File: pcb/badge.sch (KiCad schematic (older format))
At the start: 17 parts, among them IC101 CH340G, IC102 TP4056, P101 CONN_01X02, P102 USB_OTG, P103 CONN_01X05, x101 xtal_osc

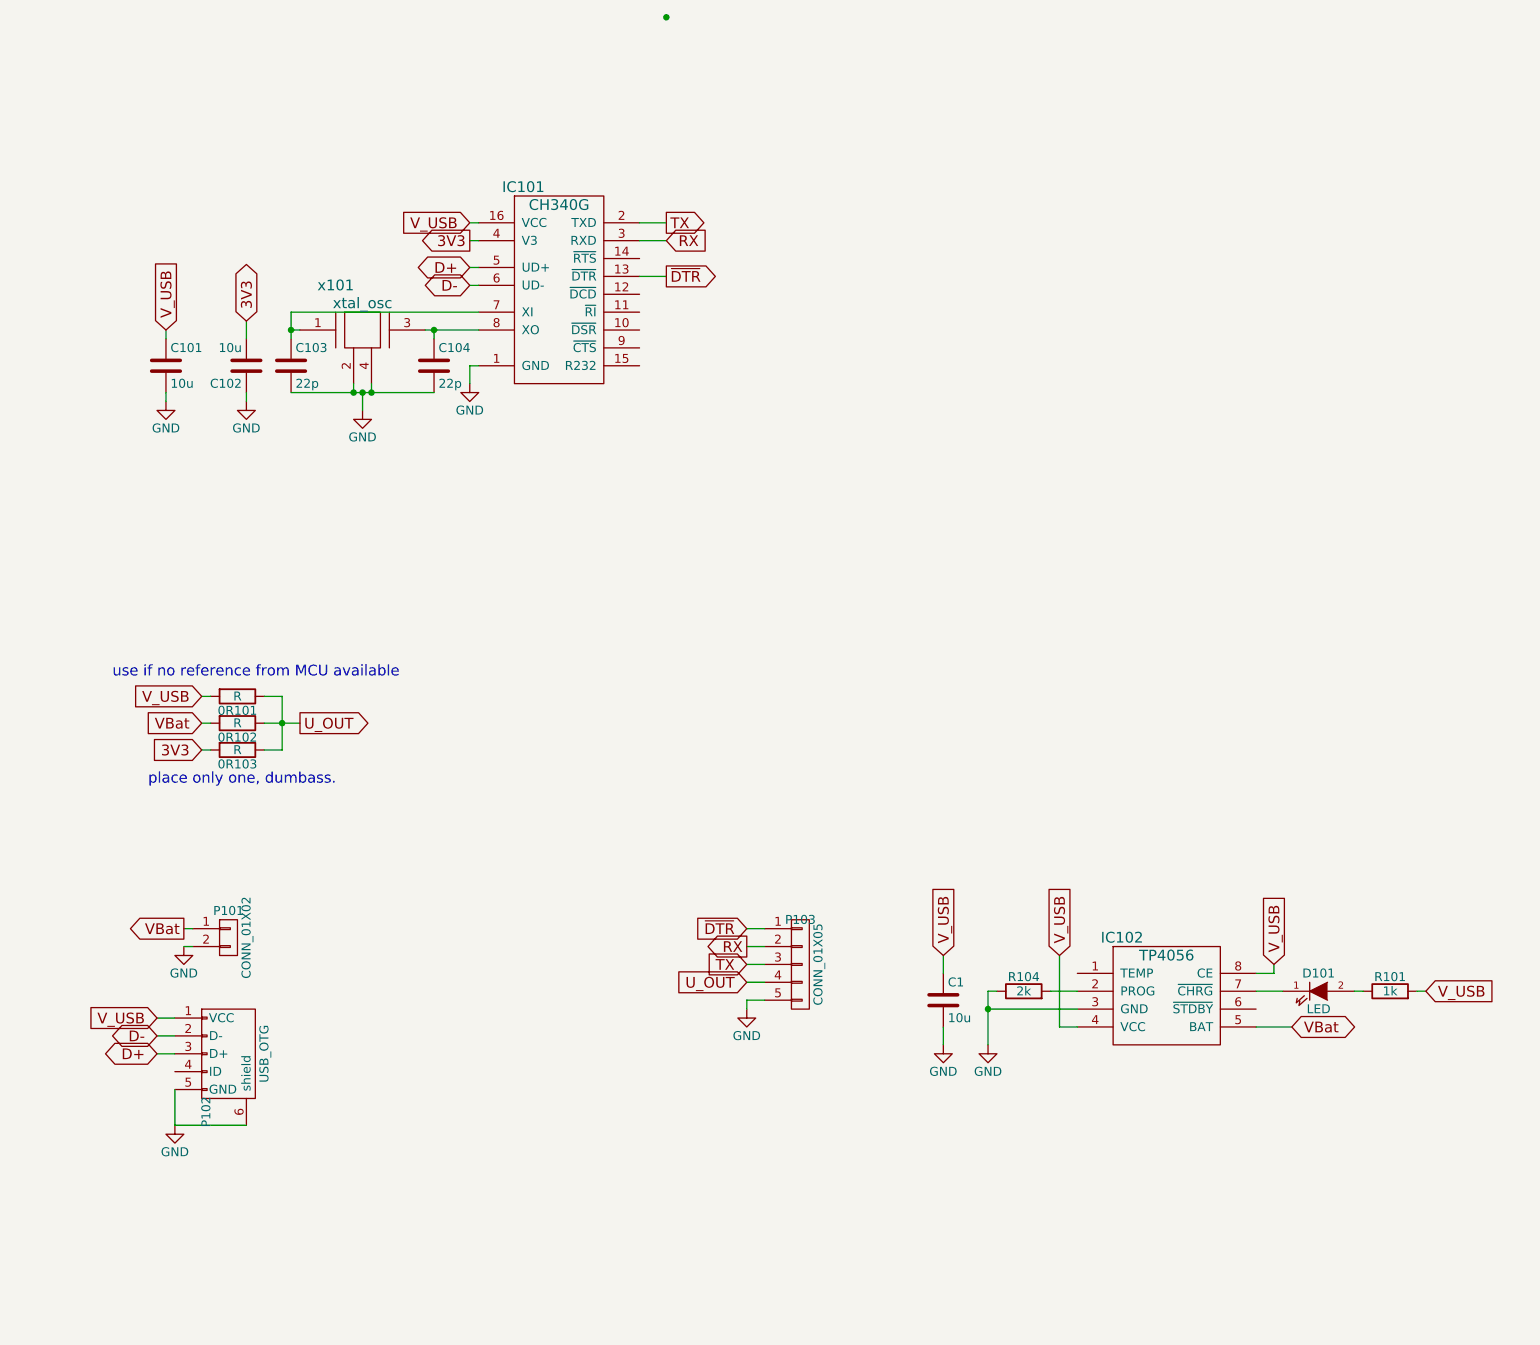
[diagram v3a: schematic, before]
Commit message: updated layout to match schema
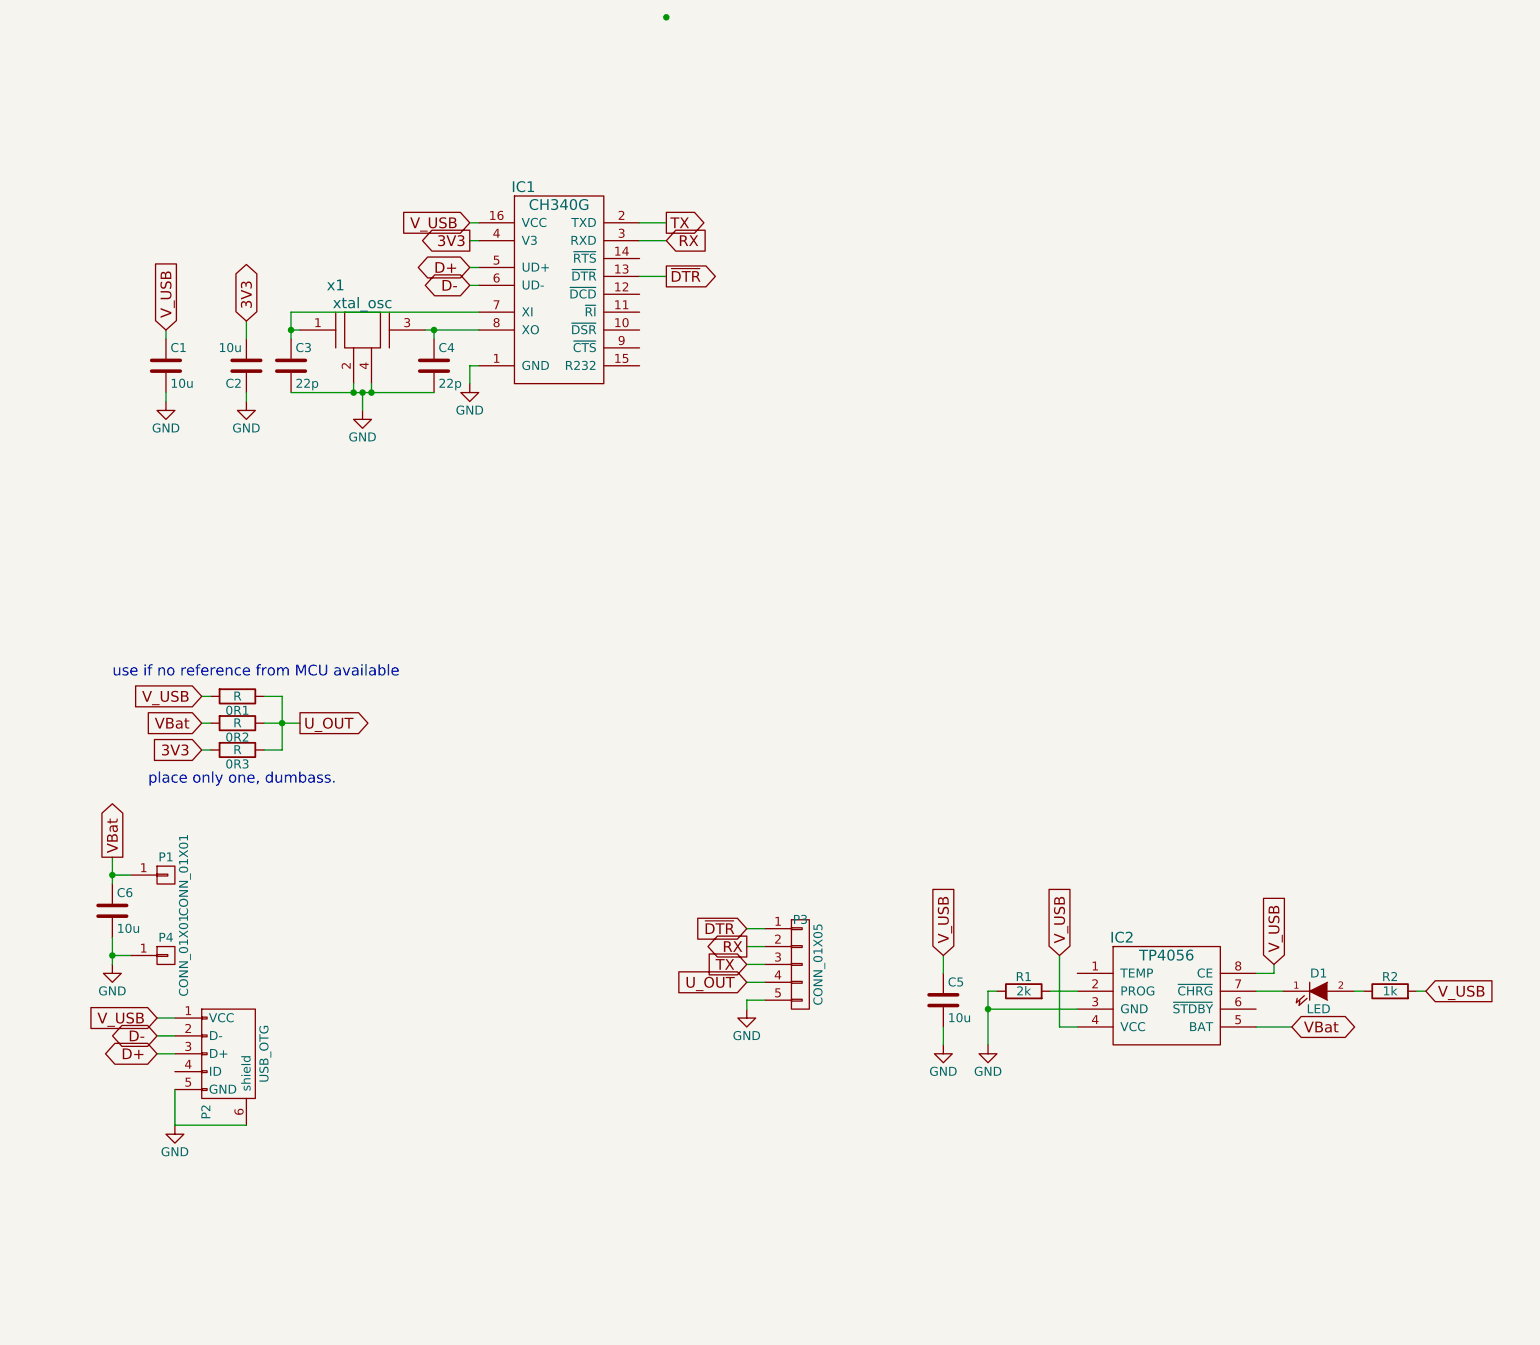
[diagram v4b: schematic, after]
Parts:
- removed P101: CONN_01X02, Pin_Headers:Pin_Header_Straight_1x02, symbol CONN_01X02
- added C6: 10u, netl:SMD_0603, symbol C
- added P1, P4: CONN_01X01, Connect:1pin, symbol CONN_01X01
- renumbered 0R101 to 0R1, 0R102 to 0R2, 0R103 to 0R3, C101 to C1, C102 to C2, C103 to C3, C104 to C4, C1 to C5, D101 to D1, IC101 to IC1, IC102 to IC2, P102 to P2, P103 to P3, R104 to R1, R101 to R2, x101 to x1
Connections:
- net GND: now also C6.2, P4.1 (P1)
- net VBat: now also C6.1, P1.1 (P1)
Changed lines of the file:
@@
 $EndDescr
 $Comp
-L CONN_01X02 P101
-U 1 1 55AEBC12
-P 1700 5450
-F 0 "P101" H 1700 5600 50  0000 C CNN
-F 1 "CONN_01X02" V 1800 5450 50  0000 C CNN
-F 2 "Pin_Headers:Pin_Header_Straight_1x02" H 1700 5450 60  0001 C CNN
-F 3 "" H 1700 5450 60  0000 C CNN
-	1    1700 5450
-	1    0    0    -1
-$EndComp
-Text GLabel 1450 5400 0    60   Output ~ 0
-VBat
-$Comp
-L GND #PWR01
-U 1 1 55AEBCB6
-P 1450 5500
-F 0 "#PWR01" H 1450 5250 50  0001 C CNN
-F 1 "GND" H 1450 5350 50  0000 C CNN
-F 2 "" H 1450 5500 60  0000 C CNN
-F 3 "" H 1450 5500 60  0000 C CNN
-	1    1450 5500
-	1    0    0    -1
-$EndComp
-$Comp
-L USB_OTG P102
+L USB_OTG P2
 U 1 1 55AEBD84
 P 1700 6100
-F 0 "P102" H 2025 5975 50  0000 C CNN
+F 0 "P2" H 2025 5975 50  0000 C CNN
 F 1 "USB_OTG" H 1700 6300 50  0000 C CNN
 F 2 "Connect:USB_Micro-B" V 1650 6000 60  0001 C CNN
@@
 V_USB
 $Comp
-L GND #PWR02
+L GND #PWR01
 U 1 1 55AEBF75
 P 1400 6500
-F 0 "#PWR02" H 1400 6250 50  0001 C CNN
+F 0 "#PWR01" H 1400 6250 50  0001 C CNN
 F 1 "GND" H 1400 6350 50  0000 C CNN
 F 2 "" H 1400 6500 60  0000 C CNN
@@
 D+
 $Comp
-L GND #PWR03
+L GND #PWR02
 U 1 1 579ECB3C
 P 1350 2450
-F 0 "#PWR03" H 1350 2200 50  0001 C CNN
+F 0 "#PWR02" H 1350 2200 50  0001 C CNN
 F 1 "GND" H 1350 2300 50  0000 C CNN
 F 2 "" H 1350 2450 50  0000 C CNN
@@
 $EndComp
 $Comp
-L C C101
+L C C1
 U 1 1 579ECCA5
 P 1350 2250
-F 0 "C101" H 1375 2350 50  0000 L CNN
+F 0 "C1" H 1375 2350 50  0000 L CNN
 F 1 "10u" H 1375 2150 50  0000 L CNN
 F 2 "netl:SMD_0603" H 1388 2100 50  0001 C CNN
@@
 $EndComp
 $Comp
-L CONN_01X05 P103
+L CONN_01X05 P3
 U 1 1 57C2DD7E
 P 4900 5600
-F 0 "P103" H 4900 5850 50  0000 C CNN
+F 0 "P3" H 4900 5850 50  0000 C CNN
 F 1 "CONN_01X05" V 5000 5600 50  0000 C CNN
 F 2 "Pin_Headers:Pin_Header_Angled_1x05" H 4900 5600 50  0001 C CNN
@@
 $EndComp
 $Comp
-L GND #PWR04
+L GND #PWR03
 U 1 1 57C2E131
 P 4600 5850
-F 0 "#PWR04" H 4600 5600 50  0001 C CNN
+F 0 "#PWR03" H 4600 5600 50  0001 C CNN
 F 1 "GND" H 4600 5700 50  0000 C CNN
 F 2 "" H 4600 5850 50  0000 C CNN
@@
 V_USB
 $Comp
-L R 0R101
+L R 0R1
 U 1 1 57C30031
 P 1750 4100
-F 0 "0R101" V 1830 4100 50  0000 C CNN
+F 0 "0R1" V 1830 4100 50  0000 C CNN
 F 1 "R" V 1750 4100 50  0000 C CNN
 F 2 "netl:SMD_0603" V 1680 4100 50  0001 C CNN
@@
 $EndComp
 $Comp
-L R 0R103
+L R 0R3
 U 1 1 57C30081
 P 1750 4400
-F 0 "0R103" V 1830 4400 50  0000 C CNN
+F 0 "0R3" V 1830 4400 50  0000 C CNN
 F 1 "R" V 1750 4400 50  0000 C CNN
 F 2 "netl:SMD_0603" V 1680 4400 50  0001 C CNN
@@
 $EndComp
 $Comp
-L R 0R102
+L R 0R2
 U 1 1 57C300C9
 P 1750 4250
-F 0 "0R102" V 1830 4250 50  0000 C CNN
+F 0 "0R2" V 1830 4250 50  0000 C CNN
 F 1 "R" V 1750 4250 50  0000 C CNN
 F 2 "netl:SMD_0603" V 1680 4250 50  0001 C CNN
@@
 use if no reference from MCU available
 $Comp
-L GND #PWR05
+L GND #PWR04
 U 1 1 57C325B8
 P 1800 2450
-F 0 "#PWR05" H 1800 2200 50  0001 C CNN
+F 0 "#PWR04" H 1800 2200 50  0001 C CNN
 F 1 "GND" H 1800 2300 50  0000 C CNN
 F 2 "" H 1800 2450 50  0000 C CNN
@@
 V_USB
 $Comp
-L CH340G IC101
+L CH340G IC1
 U 1 1 57C5C7A1
 P 3550 1850
-F 0 "IC101" H 3350 2450 60  0000 C CNN
+F 0 "IC1" H 3350 2450 60  0000 C CNN
 F 1 "CH340G" H 3550 2350 60  0000 C CNN
 F 2 "Housings_SOIC:SOIC-16_3.9x9.9mm_Pitch1.27mm" H 3550 1850 60  0001 C CNN
@@
 $EndComp
 $Comp
-L GND #PWR06
+L GND #PWR05
 U 1 1 57C5D0E9
 P 3050 2350
-F 0 "#PWR06" H 3050 2100 50  0001 C CNN
+F 0 "#PWR05" H 3050 2100 50  0001 C CNN
 F 1 "GND" H 3050 2200 50  0000 C CNN
 F 2 "" H 3050 2350 50  0000 C CNN
@@
 D+
 $Comp
-L GND #PWR07
+L GND #PWR06
 U 1 1 57C5EAC0
 P 2450 2500
-F 0 "#PWR07" H 2450 2250 50  0001 C CNN
+F 0 "#PWR06" H 2450 2250 50  0001 C CNN
 F 1 "GND" H 2450 2350 50  0000 C CNN
 F 2 "" H 2450 2500 50  0000 C CNN
@@
 $EndComp
 $Comp
-L C C103
+L C C3
 U 1 1 57C5EBA4
 P 2050 2250
-F 0 "C103" H 2075 2350 50  0000 L CNN
+F 0 "C3" H 2075 2350 50  0000 L CNN
 F 1 "22p" H 2075 2150 50  0000 L CNN
 F 2 "netl:SMD_0603" H 2088 2100 50  0001 C CNN
@@
 $EndComp
 $Comp
-L C C104
+L C C4
 U 1 1 57C5ECF7
 P 2850 2250
-F 0 "C104" H 2875 2350 50  0000 L CNN
+F 0 "C4" H 2875 2350 50  0000 L CNN
 F 1 "22p" H 2875 2150 50  0000 L CNN
 F 2 "netl:SMD_0603" H 2888 2100 50  0001 C CNN
@@
 $EndComp
 Wire Wire Line
-	1500 5500 1450 5500
-Wire Wire Line
-	1450 5400 1500 5400
-Wire Wire Line
 	1800 6500 1400 6500
 Wire Wire Line
@@
 V_USB
 $Comp
-L R R104
+L R R1
 U 1 1 57C5FAF5
 P 6150 5750
-F 0 "R104" V 6230 5750 50  0000 C CNN
+F 0 "R1" V 6230 5750 50  0000 C CNN
 F 1 "2k" V 6150 5750 50  0000 C CNN
 F 2 "netl:SMD_0603" V 6080 5750 50  0001 C CNN
@@
 	6450 5750 6300 5750
 $Comp
-L GND #PWR08
+L GND #PWR07
 U 1 1 57C5FC24
 P 5950 6050
-F 0 "#PWR08" H 5950 5800 50  0001 C CNN
+F 0 "#PWR07" H 5950 5800 50  0001 C CNN
 F 1 "GND" H 5950 5900 50  0000 C CNN
 F 2 "" H 5950 6050 50  0000 C CNN
@@
 	7450 5950 7650 5950
 $Comp
-L C C102
+L C C2
 U 1 1 57C32418
 P 1800 2250
-F 0 "C102" H 1825 2350 50  0000 L CNN
+F 0 "C2" H 1825 2350 50  0000 L CNN
 F 1 "10u" H 1825 2150 50  0000 L CNN
 F 2 "netl:SMD_0603" H 1838 2100 50  0001 C CNN
@@
 	4600 5400 4700 5400
 $Comp
-L xtal_osc x101
+L xtal_osc x1
 U 1 1 57C878D3
 P 2450 2050
-F 0 "x101" H 2300 2300 60  0000 C CNN
+F 0 "x1" H 2300 2300 60  0000 C CNN
 F 1 "xtal_osc" H 2450 2200 60  0000 C CNN
 F 2 "netl:SM_3225" H 2450 2100 60  0001 C CNN
@@
 Connection ~ 2050 2050
 $Comp
-L LED D101
+L LED D1
 U 1 1 57C893A5
 P 7800 5750
-F 0 "D101" H 7800 5850 50  0000 C CNN
+F 0 "D1" H 7800 5850 50  0000 C CNN
 F 1 "LED" H 7800 5650 50  0000 C CNN
 F 2 "netl:SMD_0603" H 7800 5750 50  0001 C CNN
@@
 $EndComp
 $Comp
-L R R101
+L R R2
 U 1 1 57C89426
 P 8200 5750
-F 0 "R101" V 8280 5750 50  0000 C CNN
+F 0 "R2" V 8280 5750 50  0000 C CNN
 F 1 "1k" V 8200 5750 50  0000 C CNN
 F 2 "netl:SMD_0603" V 8130 5750 50  0001 C CNN
@@
 	7550 5650 7550 5600
 $Comp
-L TP4056 IC102
+L TP4056 IC2
 U 1 1 57C5B388
 P 6950 5800
-F 0 "IC102" H 6700 6150 60  0000 C CNN
+F 0 "IC2" H 6700 6150 60  0000 C CNN
 F 1 "TP4056" H 6950 6050 60  0000 C CNN
 F 2 "SMD_Packages:SOIC-8-N" H 6950 5750 60  0001 C CNN
@@
 	6350 5950 6450 5950
 $Comp
-L GND #PWR09
+L GND #PWR08
 U 1 1 57DD73F7
 P 5700 6050
-F 0 "#PWR09" H 5700 5800 50  0001 C CNN
+F 0 "#PWR08" H 5700 5800 50  0001 C CNN
 F 1 "GND" H 5700 5900 50  0000 C CNN
 F 2 "" H 5700 6050 50  0000 C CNN
@@
 $EndComp
 $Comp
-L C C1
+L C C5
 U 1 1 57DD73FD
 P 5700 5800
-F 0 "C1" H 5725 5900 50  0000 L CNN
+F 0 "C5" H 5725 5900 50  0000 L CNN
 F 1 "10u" H 5725 5700 50  0000 L CNN
 F 2 "netl:SMD_0603" H 5738 5650 50  0001 C CNN
@@
 Wire Wire Line
 	5700 5550 5700 5650
+$Comp
+L C C6
+U 1 1 57F8F1E9
+P 1050 5300
+F 0 "C6" H 1075 5400 50  0000 L CNN
+F 1 "10u" H 1075 5200 50  0000 L CNN
+F 2 "netl:SMD_0603" H 1088 5150 50  0001 C CNN
+F 3 "" H 1050 5300 50  0000 C CNN
+	1    1050 5300
+	1    0    0    -1
+$EndComp
+Text GLabel 1050 5000 1    60   Output ~ 0
+VBat
+$Comp
+L GND #PWR09
+U 1 1 57F8F41D
+P 1050 5600
+F 0 "#PWR09" H 1050 5350 50  0001 C CNN
+F 1 "GND" H 1050 5450 50  0000 C CNN
+F 2 "" H 1050 5600 60  0000 C CNN
+F 3 "" H 1050 5600 60  0000 C CNN
+	1    1050 5600
+	1    0    0    -1
+$EndComp
+Wire Wire Line
+	1050 5450 1050 5600
+Wire Wire Line
+	1050 5150 1050 5000
+$Comp
+L CONN_01X01 P1
+U 1 1 57F8F79D
+P 1350 5100
+F 0 "P1" H 1350 5200 50  0000 C CNN
+F 1 "CONN_01X01" V 1450 5100 50  0000 C CNN
+F 2 "Connect:1pin" H 1350 5100 50  0001 C CNN
+F 3 "" H 1350 5100 50  0000 C CNN
+	1    1350 5100
+	1    0    0    -1
+$EndComp
+$Comp
+L CONN_01X01 P4
+U 1 1 57F8F92C
+P 1350 5550
+F 0 "P4" H 1350 5650 50  0000 C CNN
+F 1 "CONN_01X01" V 1450 5550 50  0000 C CNN
+F 2 "Connect:1pin" H 1350 5550 50  0001 C CNN
+F 3 "" H 1350 5550 50  0000 C CNN
+	1    1350 5550
+	1    0    0    -1
+$EndComp
+Wire Wire Line
+	1150 5550 1050 5550
+Connection ~ 1050 5550
+Wire Wire Line
+	1150 5100 1050 5100
+Connection ~ 1050 5100
 $EndSCHEMATC

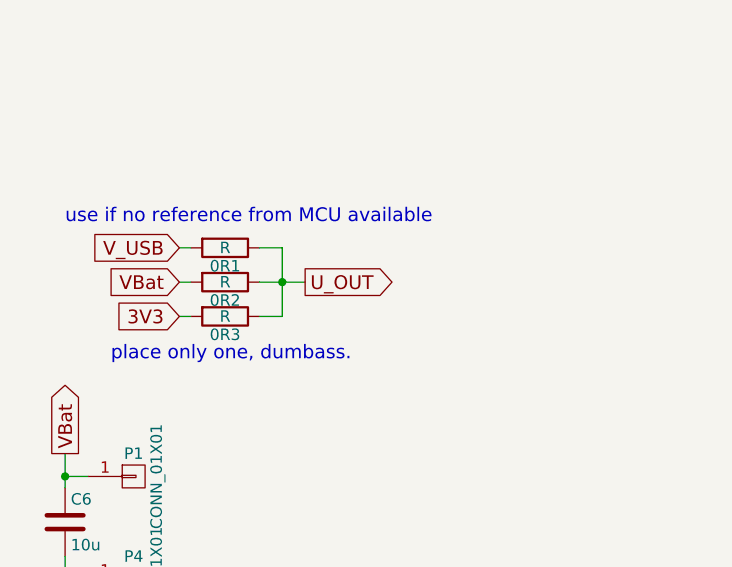
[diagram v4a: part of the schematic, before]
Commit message: removed 3V3 selection. cleaned up layout
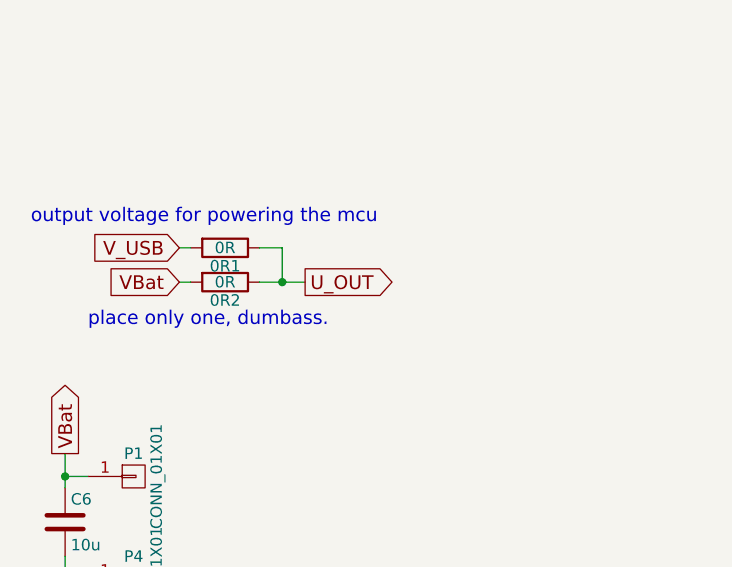
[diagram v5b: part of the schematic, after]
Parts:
- removed 0R3: R, netl:SMD_0603, symbol R
- 0R1, 0R2: value R -> 0R
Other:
- note added: "output voltage for powering the mcu"
- note removed: "use if no reference from MCU available"
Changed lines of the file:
@@
 Text GLabel 2100 4250 2    60   Output ~ 0
 U_OUT
-Text GLabel 1550 4400 0    60   Input ~ 0
-3V3
 Text GLabel 1550 4100 0    60   Input ~ 0
 V_USB
@@
 P 1750 4100
 F 0 "0R1" V 1830 4100 50  0000 C CNN
-F 1 "R" V 1750 4100 50  0000 C CNN
+F 1 "0R" V 1750 4100 50  0000 C CNN
 F 2 "netl:SMD_0603" V 1680 4100 50  0001 C CNN
 F 3 "" H 1750 4100 50  0000 C CNN
@@
 $EndComp
 $Comp
-L R 0R3
-U 1 1 57C30081
-P 1750 4400
-F 0 "0R3" V 1830 4400 50  0000 C CNN
-F 1 "R" V 1750 4400 50  0000 C CNN
-F 2 "netl:SMD_0603" V 1680 4400 50  0001 C CNN
-F 3 "" H 1750 4400 50  0000 C CNN
-	1    1750 4400
-	0    1    1    0
-$EndComp
-$Comp
 L R 0R2
 U 1 1 57C300C9
 P 1750 4250
 F 0 "0R2" V 1830 4250 50  0000 C CNN
-F 1 "R" V 1750 4250 50  0000 C CNN
+F 1 "0R" V 1750 4250 50  0000 C CNN
 F 2 "netl:SMD_0603" V 1680 4250 50  0001 C CNN
 F 3 "" H 1750 4250 50  0000 C CNN
@@
 	0    1    1    0
 $EndComp
-Text Notes 1250 4600 0    60   ~ 0
+Text Notes 1150 4450 0    60   ~ 0
 place only one, dumbass.
-Text Notes 1050 4000 0    60   ~ 0
-use if no reference from MCU available
+Text Notes 900  4000 0    60   ~ 0
+output voltage for powering the mcu
 $Comp
 L GND #PWR04
@@
 	1600 4250 1550 4250
 Wire Wire Line
-	1550 4400 1600 4400
-Wire Wire Line
 	1600 4100 1550 4100
 Wire Wire Line
 	1900 4250 2100 4250
-Wire Wire Line
-	2000 4100 2000 4400
 Connection ~ 2000 4250
-Wire Wire Line
-	2000 4400 1900 4400
 Wire Wire Line
 	1800 2450 1800 2400
@@
 	1150 5100 1050 5100
 Connection ~ 1050 5100
+Wire Wire Line
+	2000 4100 2000 4250
 $EndSCHEMATC
